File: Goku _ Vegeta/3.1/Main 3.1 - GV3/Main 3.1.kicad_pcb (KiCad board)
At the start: 2 copper layers, 215 x 206.6 mm, 43 parts, among them J1 JST-XH M1 ENC, J10 Conn_01x08_Female, J11 Motor Driver Inputs, J12 OpenMV H7, J13 JST-XH Screen, J14 Conn_01x08_Female, J15 691137710002, J16 691137710002, J17 Conn_01x08_Female, J18 Conn_01x18_Female, J19 Conn_01x10_Female, J2 JST-XH M2 ENC, J20 Conn_01x08_Female, J21 Conn_01x08_Female, J22 Conn_01x18_Female, J23 Line PCB 2, J24 B3B-XH-A(LF)(SN), J25 B2B-XH-A(LF)(SN), J3 JST-XH M3 ENC, J4 JST-XH M4 ENC, J5 XT60-M, J6 691137710002, J7 XT60-M, J8 XT60-M, J9 Line PCB 1, U1 DC-DC_Buck_Converter_7-24V_to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, U4 Adafruit_BNO055_STEMMA_QT

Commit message: move to 3.1
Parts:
- removed C3, C4: 10UF, Capacitor_SMD:C_0805_2012Metric
- removed G*** (x3): LOGO, LOGO
- removed J14, J17, J20, J21: Conn_01x08_Female, Connector_PinHeader_2.54mm:PinHeader_1x08_P2.54mm_Vertical
- removed J15, J16: 691137710002, 5mm Pitch 2-Pin Screw Terminal Block:5mm Pitch 2-Pin Screw Terminal Block
- removed J18, J22: Conn_01x18_Female, Connector_PinHeader_2.54mm:PinHeader_1x18_P2.54mm_Vertical
- removed J19: Conn_01x10_Female, Connector_PinHeader_2.54mm:PinHeader_1x10_P2.54mm_Vertical
- removed J23: Line PCB 2, Box IDC header 2x3:Box IDC header 2x3
- removed J24: B3B-XH-A(LF)(SN), B3B-XH-A_LF__SN_:JST_B3B-XH-A(LF)(SN)
- removed J25: B2B-XH-A(LF)(SN), B2B-XH-A_LF__SN_:JST_B2B-XH-A(LF)(SN)
- removed J5: XT60-M, XT60-M:XT60-M
- removed TP1: TestPoint - 5V, TestPoint:TestPoint_THTPad_D2.0mm_Drill1.0mm
- removed TP18: LOGIC_SWITCH, TestPoint:TestPoint_THTPad_D2.0mm_Drill1.0mm
- removed TP2: TestPoint - SCL, TestPoint:TestPoint_THTPad_D2.0mm_Drill1.0mm
- removed TP3: TestPoint - SDA, TestPoint:TestPoint_THTPad_D2.0mm_Drill1.0mm
- removed TP4: TestPoint - TX, TestPoint:TestPoint_THTPad_D2.0mm_Drill1.0mm
- removed TP5: TestPoint - RX, TestPoint:TestPoint_THTPad_D2.0mm_Drill1.0mm
- removed TP6: TestPoint - GND, TestPoint:TestPoint_THTPad_D2.0mm_Drill1.0mm
- added A10: ALS-PT19-315C/L177/TR8, ALS-PT19-315C_L177_TR8:XDCR_ALS-PT19-315C_L177_TR8, B.Cu at (164.1, 135.9)
- added A11: ALS-PT19-315C/L177/TR8, ALS-PT19-315C_L177_TR8:XDCR_ALS-PT19-315C_L177_TR8, B.Cu at (170.0, 150.0)
- added A12: ALS-PT19-315C/L177/TR8, ALS-PT19-315C_L177_TR8:XDCR_ALS-PT19-315C_L177_TR8, B.Cu at (164.1, 164.1)
- added A13: ALS-PT19-315C/L177/TR8, ALS-PT19-315C_L177_TR8:XDCR_ALS-PT19-315C_L177_TR8, B.Cu at (150.0, 170.0)
- added A14: ALS-PT19-315C/L177/TR8, ALS-PT19-315C_L177_TR8:XDCR_ALS-PT19-315C_L177_TR8, B.Cu at (135.9, 164.1)
- added A15: ALS-PT19-315C/L177/TR8, ALS-PT19-315C_L177_TR8:XDCR_ALS-PT19-315C_L177_TR8, B.Cu at (130.0, 150.0)
- added A16: ALS-PT19-315C/L177/TR8, ALS-PT19-315C_L177_TR8:XDCR_ALS-PT19-315C_L177_TR8, B.Cu at (135.9, 135.9)
- added A2: ALS-PT19-315C/L177/TR8, ALS-PT19-315C_L177_TR8:XDCR_ALS-PT19-315C_L177_TR8, B.Cu at (230.0, 150.0)
- added A3: ALS-PT19-315C/L177/TR8, ALS-PT19-315C_L177_TR8:XDCR_ALS-PT19-315C_L177_TR8, B.Cu at (150.0, 230.0)
- added A4: ALS-PT19-315C/L177/TR8, ALS-PT19-315C_L177_TR8:XDCR_ALS-PT19-315C_L177_TR8, B.Cu at (70.0, 150.0)
- added A5: ALS-PT19-315C/L177/TR8, ALS-PT19-315C_L177_TR8:XDCR_ALS-PT19-315C_L177_TR8, B.Cu at (150.0, 100.0)
- added A6: ALS-PT19-315C/L177/TR8, ALS-PT19-315C_L177_TR8:XDCR_ALS-PT19-315C_L177_TR8, B.Cu at (200.0, 150.0)
- added A7: ALS-PT19-315C/L177/TR8, ALS-PT19-315C_L177_TR8:XDCR_ALS-PT19-315C_L177_TR8, B.Cu at (150.0, 200.0)
- added A8: ALS-PT19-315C/L177/TR8, ALS-PT19-315C_L177_TR8:XDCR_ALS-PT19-315C_L177_TR8, B.Cu at (100.0, 150.0)
- added A9: ALS-PT19-315C/L177/TR8, ALS-PT19-315C_L177_TR8:XDCR_ALS-PT19-315C_L177_TR8, B.Cu at (150.0, 130.0)
- added C10: 1uF, Capacitor_SMD:C_0805_2012Metric, F.Cu at (148.2, 145.6)
- added C11: 100uF, Capacitor_THT:CP_Radial_D10.0mm_P5.00mm, F.Cu at (184.6, 85.0)
- added C12: 560uF, Capacitor_THT:CP_Radial_D18.0mm_P7.50mm, F.Cu at (124.8, 84.5)
- added C13: 560uF, Capacitor_THT:CP_Radial_D18.0mm_P7.50mm, F.Cu at (175.2, 84.5)
- added C14: 100uF, Capacitor_THT:CP_Radial_D10.0mm_P5.00mm, F.Cu at (115.4, 85.0)
- added C2: 100uF, Capacitor_THT:CP_Radial_D10.0mm_P5.00mm, F.Cu at (165.6, 197.0)
- added C9: 100uF, Capacitor_THT:CP_Radial_D10.0mm_P5.00mm, F.Cu at (152.4, 162.5)
- added D3: SS510, Diode_SMD:D_SMC, F.Cu at (144.2, 151.8)
- added D4: STTH2002G-TR, Package_TO_SOT_SMD:TO-263-2, F.Cu at (168.0, 100.2)
- added L3: 56uH, Inductor_SMD:L_Bourns_SRR1260, F.Cu at (134.0, 150.0)
- added LED1: JB2835AWT-W-U30GA0000-N0000001, JB2835AWT-W-U30GA0000-N0000001:LED_J2835_CRW, B.Cu at (150.0, 73.0)
- added LED10: JB2835AWT-W-U30GA0000-N0000001, JB2835AWT-W-U30GA0000-N0000001:LED_J2835_CRW, B.Cu at (162.0, 138.0)
- added LED11: JB2835AWT-W-U30GA0000-N0000001, JB2835AWT-W-U30GA0000-N0000001:LED_J2835_CRW, B.Cu at (167.0, 150.0)
- added LED12: JB2835AWT-W-U30GA0000-N0000001, JB2835AWT-W-U30GA0000-N0000001:LED_J2835_CRW, B.Cu at (162.0, 162.0)
- added LED13: JB2835AWT-W-U30GA0000-N0000001, JB2835AWT-W-U30GA0000-N0000001:LED_J2835_CRW, B.Cu at (150.0, 167.0)
- added LED14: JB2835AWT-W-U30GA0000-N0000001, JB2835AWT-W-U30GA0000-N0000001:LED_J2835_CRW, B.Cu at (138.0, 162.0)
- added LED15: JB2835AWT-W-U30GA0000-N0000001, JB2835AWT-W-U30GA0000-N0000001:LED_J2835_CRW, B.Cu at (133.0, 150.0)
- added LED16: JB2835AWT-W-U30GA0000-N0000001, JB2835AWT-W-U30GA0000-N0000001:LED_J2835_CRW, B.Cu at (138.0, 138.0)
- added LED2: JB2835AWT-W-U30GA0000-N0000001, JB2835AWT-W-U30GA0000-N0000001:LED_J2835_CRW, B.Cu at (227.0, 150.0)
- added LED3: JB2835AWT-W-U30GA0000-N0000001, JB2835AWT-W-U30GA0000-N0000001:LED_J2835_CRW, B.Cu at (150.0, 227.0)
- added LED4: JB2835AWT-W-U30GA0000-N0000001, JB2835AWT-W-U30GA0000-N0000001:LED_J2835_CRW, B.Cu at (73.0, 150.0)
- added LED5: JB2835AWT-W-U30GA0000-N0000001, JB2835AWT-W-U30GA0000-N0000001:LED_J2835_CRW, B.Cu at (150.0, 103.0)
- added LED6: JB2835AWT-W-U30GA0000-N0000001, JB2835AWT-W-U30GA0000-N0000001:LED_J2835_CRW, B.Cu at (197.0, 150.0)
- added LED7: JB2835AWT-W-U30GA0000-N0000001, JB2835AWT-W-U30GA0000-N0000001:LED_J2835_CRW, B.Cu at (150.0, 197.0)
- added LED8: JB2835AWT-W-U30GA0000-N0000001, JB2835AWT-W-U30GA0000-N0000001:LED_J2835_CRW, B.Cu at (103.0, 150.0)
- added LED9: JB2835AWT-W-U30GA0000-N0000001, JB2835AWT-W-U30GA0000-N0000001:LED_J2835_CRW, B.Cu at (150.0, 133.0)
- added Q1: BSC040N10NS5, Package_TO_SOT_SMD:TDSON-8-1, F.Cu at (133.2, 108.0)
- added R1: 12R, Resistor_SMD:R_0805_2012Metric, B.Cu at (154.0, 73.0)
- added R10: 10K, Resistor_SMD:R_0805_2012Metric, B.Cu at (227.0, 146.0)
- added R11: 10K, Resistor_SMD:R_0805_2012Metric, B.Cu at (154.0, 227.0)
- added R12: 10K, Resistor_SMD:R_0805_2012Metric, B.Cu at (73.0, 154.0)
- added R15: 10K, Resistor_SMD:R_0805_2012Metric, B.Cu at (154.0, 197.0)
- added R16: 10K, Resistor_SMD:R_0805_2012Metric, B.Cu at (103.0, 154.0)
- added R17: 12R, Resistor_SMD:R_0805_2012Metric, B.Cu at (154.0, 133.0)
- added R18: 12R, Resistor_SMD:R_0805_2012Metric, B.Cu at (164.8, 140.8)
- added R19: 12R, Resistor_SMD:R_0805_2012Metric, B.Cu at (167.0, 154.0)
- added R2: 12R, Resistor_SMD:R_0805_2012Metric, B.Cu at (227.0, 154.0)
- added R20: 12R, Resistor_SMD:R_0805_2012Metric, B.Cu at (159.2, 164.8)
- added R21: 12R, Resistor_SMD:R_0805_2012Metric, B.Cu at (146.0, 167.0)
- added R22: 12R, Resistor_SMD:R_0805_2012Metric, B.Cu at (135.2, 159.2)
- added R23: 12R, Resistor_SMD:R_0805_2012Metric, B.Cu at (133.0, 146.0)
- added R24: 12R, Resistor_SMD:R_0805_2012Metric, B.Cu at (140.8, 135.2)
- added R25: 10K, Resistor_SMD:R_0805_2012Metric, B.Cu at (146.0, 133.0)
- added R26: 10K, Resistor_SMD:R_0805_2012Metric, B.Cu at (159.2, 135.2)
- added R27: 10K, Resistor_SMD:R_0805_2012Metric, B.Cu at (167.0, 146.0)
- added R28: 10K, Resistor_SMD:R_0805_2012Metric, B.Cu at (164.8, 159.2)
- added R29: 10K, Resistor_SMD:R_0805_2012Metric, B.Cu at (154.0, 167.0)
- added R3: 12R, Resistor_SMD:R_0805_2012Metric, B.Cu at (146.0, 227.0)
- added R30: 10K, Resistor_SMD:R_0805_2012Metric, B.Cu at (140.8, 164.8)
- added R31: 10K, Resistor_SMD:R_0805_2012Metric, B.Cu at (133.0, 154.0)
- added R32: 10K, Resistor_SMD:R_0805_2012Metric, B.Cu at (135.2, 140.8)
- added R35: 2K94, Resistor_SMD:R_0805_2012Metric, F.Cu at (151.7, 145.6)
- added R36: 1K5, Resistor_SMD:R_0805_2012Metric, F.Cu at (151.7, 156.1)
- added R37: CT6EP103, POT_CT-6EP_NDC:POT_CT-6EP_NDC, F.Cu at (159.8, 141.4)
- added R38: 57K, Resistor_SMD:R_0805_2012Metric, F.Cu at (148.2, 143.6)
- added R4: 12R, Resistor_SMD:R_0805_2012Metric, B.Cu at (73.0, 146.0)
- added R5: 12R, Resistor_SMD:R_0805_2012Metric, B.Cu at (154.0, 103.0)
- added R6: 12R, Resistor_SMD:R_0805_2012Metric, B.Cu at (197.0, 154.0)
- added R7: 12R, Resistor_SMD:R_0805_2012Metric, B.Cu at (146.0, 197.0)
- added R8: 12R, Resistor_SMD:R_0805_2012Metric, B.Cu at (103.0, 146.0)
- added R9: 10K, Resistor_SMD:R_0805_2012Metric, B.Cu at (146.0, 73.0)
- added U2: ~, Converter_DCDC:DC-DC Multi-output Buck Converter, F.Cu at (163.3, 230.0)
- added U3: LM2587S-ADJ, LM2587S-ADJ:VREG_TPS79625KTTR, F.Cu at (160.6, 150.9)
- added U5: TB67H420FTG Dual/Single Motor Driver Carrier, TB67H420FTG Dual_Single Motor Driver Carrier:TB67H420FTG DualSingle Motor Driver Carrier, F.Cu at (200.0, 150.0)
- added U6: TB67H420FTG Dual/Single Motor Driver Carrier, TB67H420FTG Dual_Single Motor Driver Carrier:TB67H420FTG DualSingle Motor Driver Carrier, F.Cu at (100.0, 150.0)
- added U7: TB67H420FTG Dual/Single Motor Driver Carrier, TB67H420FTG Dual_Single Motor Driver Carrier:TB67H420FTG DualSingle Motor Driver Carrier, F.Cu at (70.0, 150.0)
- added U8: DEV-16771, DEV-16771:MODULE_DEV-16771, F.Cu at (150.0, 218.0)
- A1: value A000067 -> ALS-PT19-315C/L177/TR8; footprint A000067:ARDUINO_A000067_FLIPPED -> ALS-PT19-315C_L177_TR8:XDCR_ALS-PT19-315C_L177_TR8; moved to B.Cu
- C1: value 10UF -> 100uF; footprint Capacitor_SMD:C_0805_2012Metric -> Capacitor_THT:CP_Radial_D10.0mm_P5.00mm
- J1: value JST-XH M1 ENC -> BATTERY POWER; footprint B4B-XH-A_LF__SN_:JST_B4B-XH-A(LF)(SN) -> Connector_AMASS:AMASS_XT30U-F_1x02_P5.0mm_Vertical
- J10: value Conn_01x08_Female -> Motor 4; footprint Connector_PinHeader_2.54mm:PinHeader_1x08_P2.54mm_Vertical -> Connector_PinSocket_2.54mm:PinSocket_1x06_P2.54mm_Vertical
- J11: value Motor Driver Inputs -> LEFT HEADERS; footprint Box IDC header 2x5:Box IDC header 2x5 -> Connector_PinHeader_2.54mm:PinHeader_1x24_P2.54mm_Vertical
- J12: value OpenMV H7 -> RIGHT HEADERS; footprint Box IDC header 2x3:Box IDC header 2x3 -> Connector_PinHeader_2.54mm:PinHeader_1x24_P2.54mm_Vertical
- J13: value JST-XH Screen -> MID HEADERS; footprint B4B-XH-A_LF__SN_:JST_B4B-XH-A(LF)(SN) -> Connector_PinHeader_2.54mm:PinHeader_1x05_P2.54mm_Vertical
- J2: value JST-XH M2 ENC -> BACKUP 5V; footprint B4B-XH-A_LF__SN_:JST_B4B-XH-A(LF)(SN) -> Connector_AMASS:AMASS_XT30U-F_1x02_P5.0mm_Vertical
- J3: value JST-XH M3 ENC -> BACKUP 3V3; footprint B4B-XH-A_LF__SN_:JST_B4B-XH-A(LF)(SN) -> Connector_AMASS:AMASS_XT30U-F_1x02_P5.0mm_Vertical
- J4: value JST-XH M4 ENC -> I2C; footprint B4B-XH-A_LF__SN_:JST_B4B-XH-A(LF)(SN) -> Connector_AMASS:AMASS_XT30U-F_1x02_P5.0mm_Vertical
- J6: value 691137710002 -> Solenoid; footprint 5mm Pitch 2-Pin Screw Terminal Block:5mm Pitch 2-Pin Screw Terminal Block -> TerminalBlock:TerminalBlock_bornier-2_P5.08mm
- J7: value XT60-M -> Motor 1; footprint XT60-M:XT60-M -> Connector_PinSocket_2.54mm:PinSocket_1x06_P2.54mm_Vertical
- J8: value XT60-M -> Motor 2; footprint XT60-M:XT60-M -> Connector_PinSocket_2.54mm:PinSocket_1x06_P2.54mm_Vertical
- J9: value Line PCB 1 -> Motor 3; footprint Box IDC header 2x3:Box IDC header 2x3 -> Connector_PinSocket_2.54mm:PinSocket_1x06_P2.54mm_Vertical
- R13, R14: moved to B.Cu
- U1: value DC-DC_Buck_Converter_7-24V_to_5V_4A -> ~; footprint 2.3 PCBs:DC-DC_Buck_Converter_7-24V_to_5V_4A -> Converter_DCDC:DC-DC Multi-output Buck Converter
- U4: value Adafruit_BNO055_STEMMA_QT -> TB67H420FTG Dual/Single Motor Driver Carrier; footprint 2.3 PCBs:Adafruit IMU BNO055 -> TB67H420FTG Dual_Single Motor Driver Carrier:TB67H420FTG DualSingle Motor Driver Carrier
- moved J10 138.9 mm to (95.5, 120.5), turned to 45 degrees
- moved J4 128.9 mm to (78.8, 175.5), turned to 0 degrees
- moved J6 124.8 mm to (128.5, 101.6), turned to 90 degrees
- moved J1 121.6 mm to (78.8, 124.5)
- moved U4 111.4 mm to (230.0, 150.0), turned to 0 degrees
- moved J11 96.9 mm to (161.0, 247.2), turned to 180 degrees
- moved R14 90.6 mm to (197.0, 146.0), turned to 0 degrees
- moved J7 89.2 mm to (204.5, 120.5), turned to -45 degrees
- moved C1 88.3 mm to (128.6, 197.0), turned to 0 degrees
- moved J13 88.1 mm to (144.9, 183.5)
- moved J12 82.8 mm to (139.0, 247.2), turned to 180 degrees
- moved U1 81.0 mm to (116.8, 230.0), turned to 90 degrees
- moved A1 61.0 mm to (150.0, 70.0), turned to 180 degrees
- moved J8 53.5 mm to (204.5, 179.5), turned to -135 degrees
- moved J2 45.1 mm to (221.2, 124.5), turned to 180 degrees
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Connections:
- A1 pad 1: Net-(A1-Pad1) -> +3V3
- A1 pad 2: /M3ENCA -> /21
- C1 pad 1: +5V -> GND
- C1 pad 2: GND -> +3V3
- J1 pad 1: /M1ENCB -> GND
- J1 pad 2: /M1ENCA -> +15V
- J10 pad 1: Net-(A1-PadNC) -> Net-(J10-Pin_1)
- J10 pad 2: Net-(A1-PadIOREF) -> Net-(J10-Pin_2)
- J10 pad 3: Net-(A1-PadRESET) -> GND
- J10 pad 4: Net-(A1-Pad3V3) -> +3V3
- J10 pad 5: +5V -> /32
- J10 pad 6: GND -> /28
- J11 pad 1: /DIR1 (1) -> GND
- J11 pad 10: GND -> /8
- J11 pad 2: /PWM1 (1) -> /0
- J11 pad 3: /DIR2 (2) -> /1
- J11 pad 4: /PWM2 (2) -> /2
- J11 pad 5: GND -> /3
- J11 pad 6: /DIR1 (3) -> /4
- J11 pad 7: /PWM1 (3) -> /5
- J11 pad 8: /DIR2 (4) -> /6
- J11 pad 9: /PWM2 (4) -> /7
- J12 pad 3: /TX -> +3V3
- J12 pad 4: /RX -> /23
- J12 pad 5: unconnected-(J12-Pad5) -> /22
- J12 pad 6: unconnected-(J12-Pad6) -> /21
- J13 pad 1: +5V -> /ON/OFF
- J13 pad 2: GND -> /PROGRAM
- J13 pad 3: /SCL -> GND
- J13 pad 4: /SDA -> unconnected-(J13-Pin_4-Pad4)
- J2 pad 1: /M2ENCB -> GND
- J2 pad 2: /M2ENCA -> +5V
- J3 pad 1: /M3ENCB -> GND
- J3 pad 2: /M3ENCA -> +3V3
- J4 pad 1: /M4ENCB -> /19
- J4 pad 2: /M4ENCA -> /18
- J6 pad 1: +15V -> Net-(D3-K)
- J6 pad 2: GND -> Net-(D4-K)
- J9 pad 1: Net-(A1-PadAD0) -> Net-(J9-Pin_1)
- J9 pad 2: Net-(A1-PadAD1) -> Net-(J9-Pin_2)
- J9 pad 3: Net-(A1-PadAD2) -> GND
- J9 pad 4: Net-(A1-PadAD3) -> +3V3
- J9 pad 5: Net-(A1-PadAD4) -> /34
- J9 pad 6: Net-(A1-PadAD5) -> /33
- R13 pad 1: /SCL -> GND
- R13 pad 2: +5V -> /20
- R14 pad 1: /SDA -> GND
- R14 pad 2: +5V -> /27
- U1 pad 4: +5V -> +3V3
- U4 pad 1: +5V -> unconnected-(U4-VM-Pad1)
- U4 pad 2: unconnected-(U4-Pad2) -> GND
- U4 pad 3: GND -> unconnected-(U4-VCC-Pad3)
- U4 pad 4: /SCL -> /4
- U4 pad 5: /SDA -> /3
- U4 pad 6: /RST -> /2
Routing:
- net +3V3: track 0.00 -> 760.4 mm, vias 0 -> 13
- net Net-(J7-PadN): track 239.2 -> 0.00 mm
- net Net-(D3-K): track 0.00 -> 200.8 mm, vias 0 -> 3
- net /SDA: track 192.6 -> 0.00 mm, vias 1 -> 0
- net /21: track 0.00 -> 190.6 mm
- net +5V: track 30.4 -> 220.0 mm, vias 1 -> 0
- net /SCL: track 179.9 -> 0.00 mm, vias 2 -> 0
- net /TX: track 168.8 -> 0.00 mm, vias 1 -> 0
- net /RX: track 165.6 -> 0.00 mm
- net Net-(A1-PadAD6): track 161.1 -> 0.00 mm
- net Net-(A1-PadAD7): track 156.3 -> 0.00 mm
- net Net-(A1-PadAD3): track 152.7 -> 0.00 mm
- net Net-(A1-PadAD0): track 152.4 -> 0.00 mm
- net /20: track 0.00 -> 152.0 mm
- net Net-(A1-PadAD8): track 151.5 -> 0.00 mm, vias 2 -> 0
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- added copper zone on F.Cu, net +15V
- added copper zone on B.Cu, net GND
- removed copper zone on B.Cu, net +5V
- removed copper zone on F.Cu, net GND
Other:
- board size 215 x 206.6 mm -> 206 x 197.4 mm
- board text added: "Designed by Hugh Phan - September 2023"
- board text added: "Fort Street's Team Silverback Hugh Phan Jayden Nguyen Issey Lee Jack Sumner KZ KC"
- board text added: "MOTOR A"
- board text added: "MOTOR B"
- board text added: "MOTOR C"
- board text added: "MOTOR D"
- board text added: "TEENSY 4.1 3V3 LINES NOT CONNECTED"
- board text removed: "15V"
- board text removed: "3V3"
- board text removed: "5V"
- board text removed: "Designed by Hugh Phan 9/07/2023"
- board text removed: "Fort Street Team Silverback 2023 Hugh Phan Issey Lee Jayden Nguyen Jack Sumner"
- board text removed: "G V 2"
- board text removed: "GND"
- board text removed: "LINE PCB"
- board text removed: "LOGIC"
- board text removed: "MAIN 2.4 PCB"
- board text removed: "RX"
- board text removed: "SCL"
- board text removed: "SDA"
- board text removed: "SEN1"
- board text removed: "TX"
- board text removed: "X"

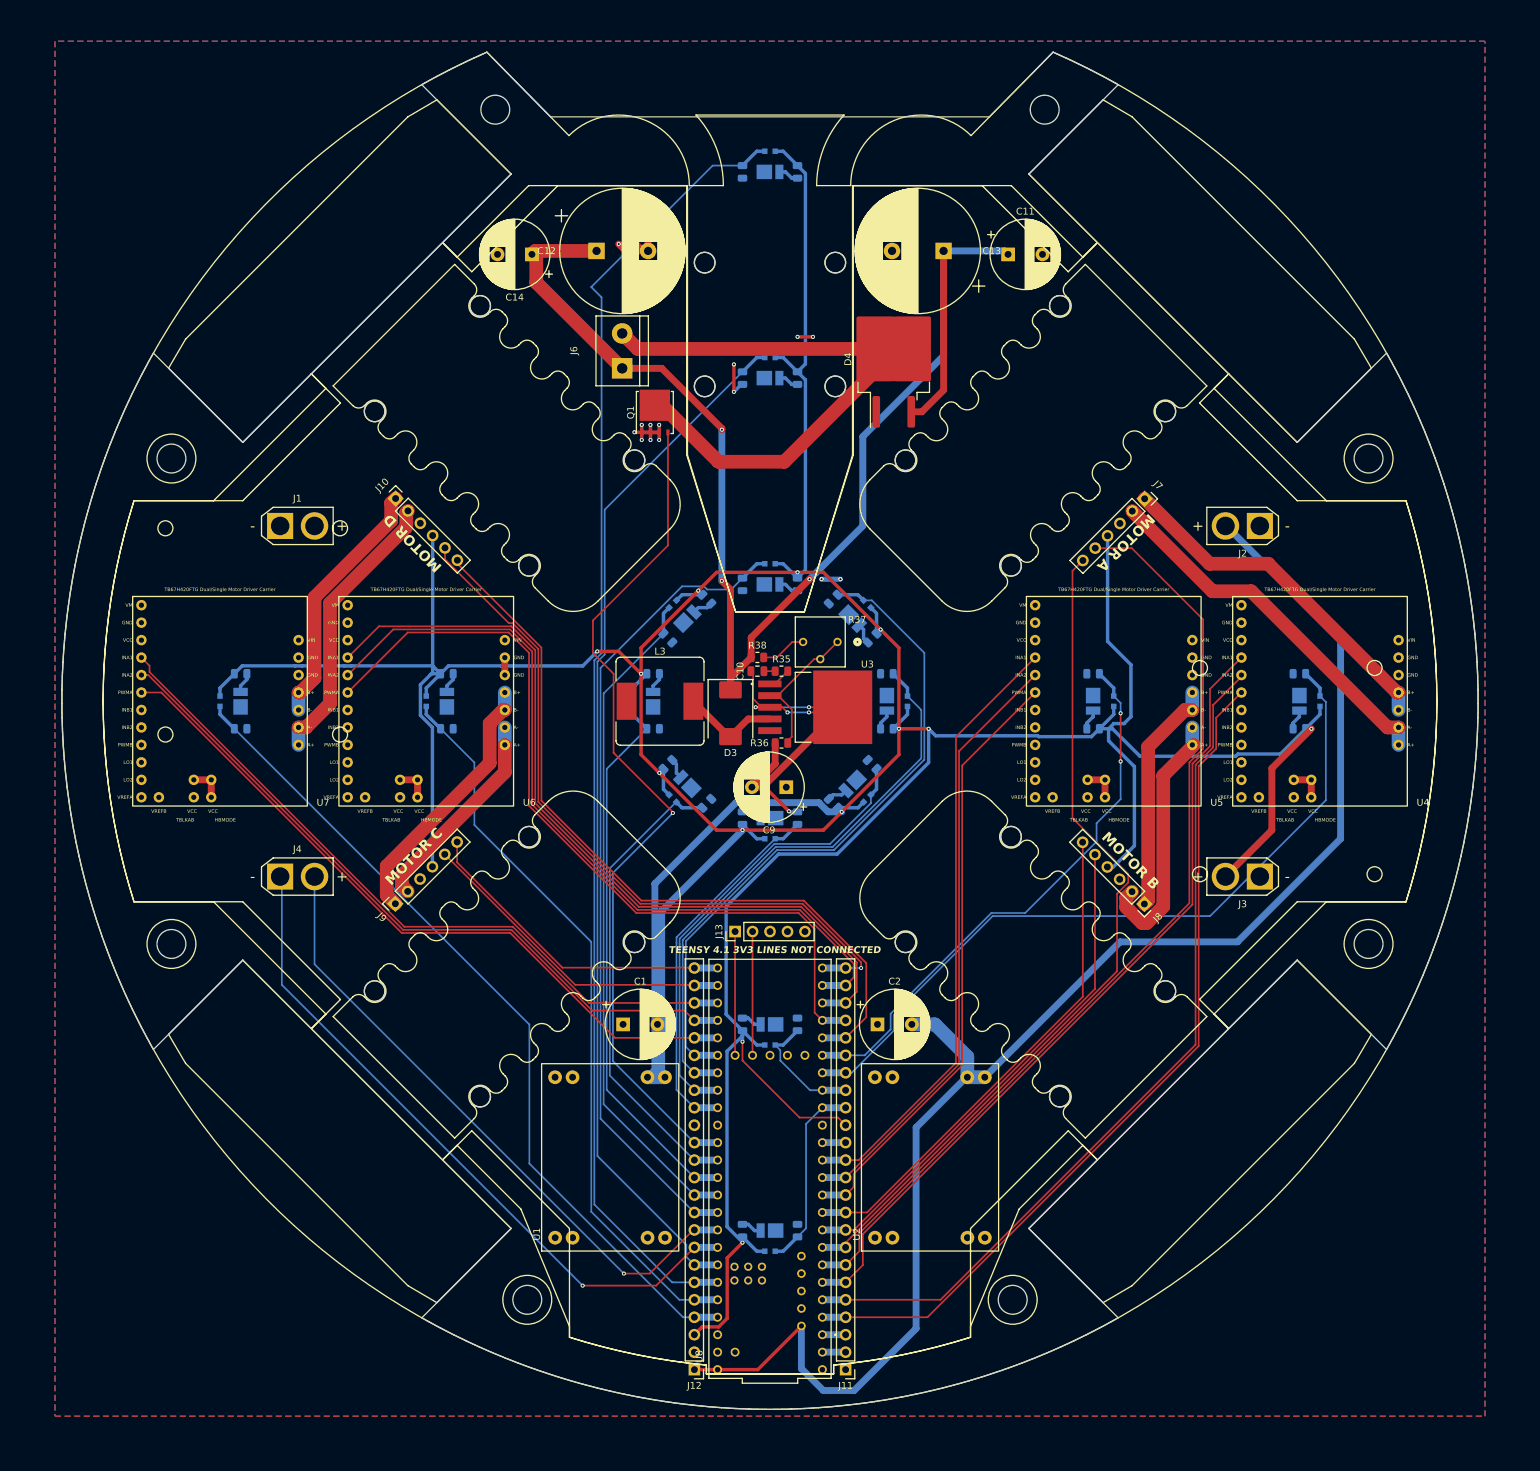
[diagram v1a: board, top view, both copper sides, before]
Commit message: MAIN 3.1 DONE no silkscreen
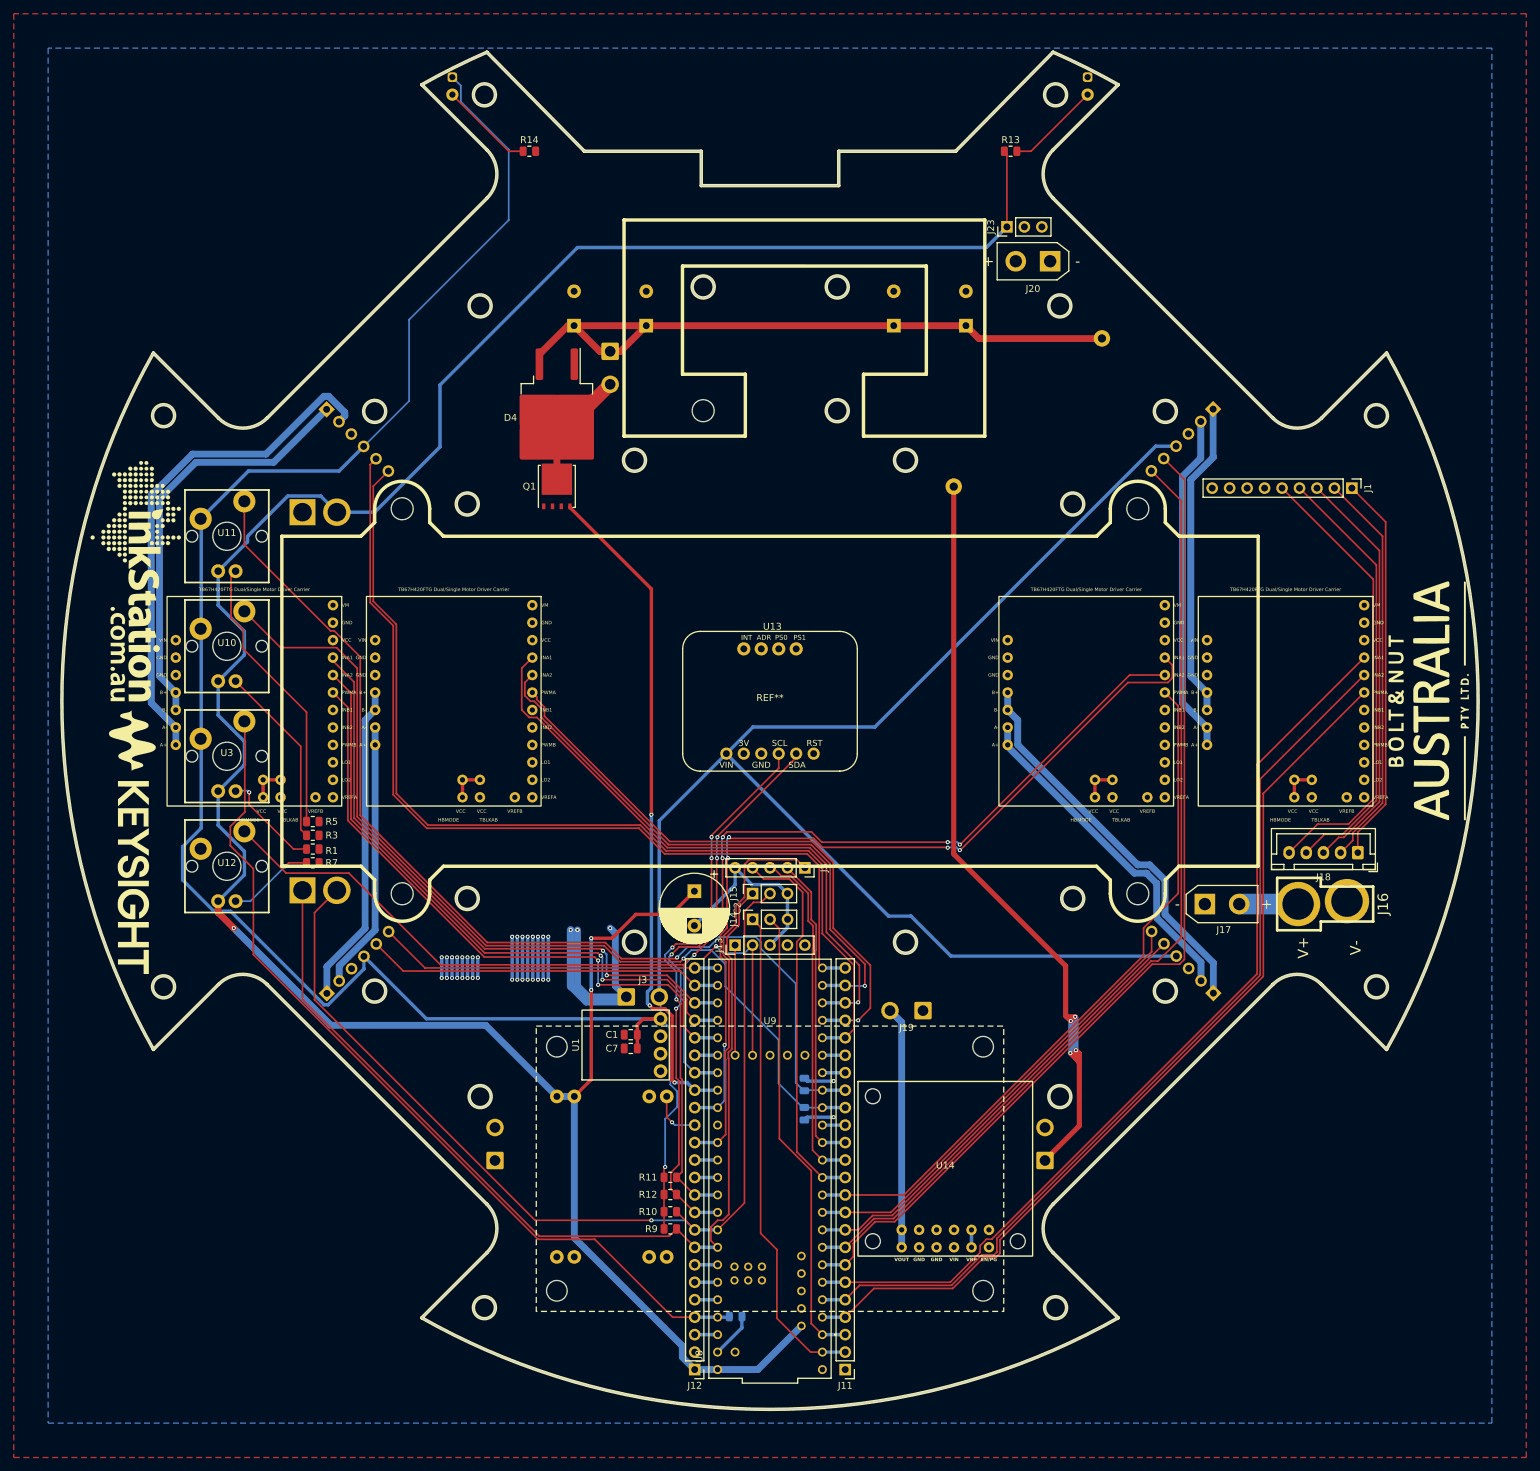
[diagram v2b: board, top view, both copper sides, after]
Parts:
- removed A1, A10, A11, A12, A13, A14, A15, A16, A2, A3, A4, A5, A6, A7, A8, A9: ALS-PT19-315C/L177/TR8, ALS-PT19-315C_L177_TR8:XDCR_ALS-PT19-315C_L177_TR8
- removed C10: 1uF, Capacitor_SMD:C_0805_2012Metric
- removed C11, C14, C9: 100uF, Capacitor_THT:CP_Radial_D10.0mm_P5.00mm
- removed C12, C13: 560uF, Capacitor_THT:CP_Radial_D18.0mm_P7.50mm
- removed D3: SS510, Diode_SMD:D_SMC
- removed L3: 56uH, Inductor_SMD:L_Bourns_SRR1260
- removed LED1, LED10, LED11, LED12, LED13, LED14, LED15, LED16, LED2, LED3, LED4, LED5, LED6, LED7, LED8, LED9: JB2835AWT-W-U30GA0000-N0000001, JB2835AWT-W-U30GA0000-N0000001:LED_J2835_CRW
- removed R16, R25, R26, R27, R28, R29, R30, R31, R32: 10K, Resistor_SMD:R_0805_2012Metric
- removed R17, R18, R19, R20, R21, R22, R23, R24, R8: 12R, Resistor_SMD:R_0805_2012Metric
- removed R35: 2K94, Resistor_SMD:R_0805_2012Metric
- removed R36: 1K5, Resistor_SMD:R_0805_2012Metric
- removed R37: CT6EP103, POT_CT-6EP_NDC:POT_CT-6EP_NDC
- removed R38: 57K, Resistor_SMD:R_0805_2012Metric
- added C3: 750uF, Capacitor_THT:CP_Radial_D10.0mm_P5.00mm, B.Cu at (121.5, 95.4)
- added C4: 750uF, Capacitor_THT:CP_Radial_D10.0mm_P5.00mm, B.Cu at (132.0, 95.4)
- added C5: 750uF, Capacitor_THT:CP_Radial_D10.0mm_P5.00mm, B.Cu at (168.0, 95.4)
- added C6: 750uF, Capacitor_THT:CP_Radial_D10.0mm_P5.00mm, B.Cu at (178.5, 95.4)
- added C7: 10uF, Capacitor_SMD:C_0805_2012Metric, F.Cu at (129.8, 200.5)
- added D1: LED, LED_THT:LED_D3.0mm, B.Cu at (196.2, 59.2)
- added G***: LOGO, LOGO, F.Cu at (245.5, 150.0)
- added G***: LOGO, LOGO, F.Cu at (57.2, 170.5)
- added G***: LOGO, LOGO, F.Cu at (57.8, 132.5)
- added J14: UART, Connector_PinSocket_2.54mm:PinSocket_1x03_P2.54mm_Vertical, F.Cu at (147.5, 181.7)
- added J15: I2C, Connector_PinSocket_2.54mm:PinSocket_1x03_P2.54mm_Vertical, F.Cu at (147.5, 178.0)
- added J16: 4S Battery, Connectors:DEANS, F.Cu at (231.4, 179.5)
- added J17: Power Switch, Connector_AMASS:AMASS_XT30UPB-F_1x02_P5.0mm_Vertical, F.Cu at (213.2, 179.5)
- added J18: Batt Bal, Connector_JST:JST_XH_B5B-XH-A_1x05_P2.50mm_Vertical, F.Cu at (235.5, 172.0)
- added J19: 5V PI, Connector_Wire:SolderWire-0.75sqmm_1x02_P4.8mm_D1.25mm_OD2.3mm, F.Cu at (172.2, 195.0)
- added J20: ESC PWR, Connector_AMASS:AMASS_XT30UPB-F_1x02_P5.0mm_Vertical, F.Cu at (190.8, 86.0)
- added J23: ESC PWM, Connector_PinHeader_2.54mm:PinHeader_1x03_P2.54mm_Vertical, F.Cu at (184.5, 81.0)
- added J5: SPI, Connector_PinSocket_2.54mm:PinSocket_1x05_P2.54mm_Vertical, F.Cu at (155.1, 174.2)
- added Q2: Q_Photo_NPN, LED_THT:LED_D3.0mm, B.Cu at (103.8, 59.2)
- added REF**: Main 3.1 3D Model, 2.3 PCBs:Main 3.1 3D Model, F.Cu at (150.0, 150.0)
- added U10: ~, Button_Switch_Keyboard:SW_Cherry_MX_3mmLED, F.Cu at (71.0, 142.0)
- added U11: ~, Button_Switch_Keyboard:SW_Cherry_MX_3mmLED, F.Cu at (71.0, 126.0)
- added U12: ~, Button_Switch_Keyboard:SW_Cherry_MX_3mmLED, F.Cu at (71.0, 174.0)
- added U13: Adafruit_BNO055_STEMMA_QT, 2.3 PCBs:Adafruit IMU BNO055, F.Cu at (150.0, 150.0)
- added U14: ~, Converter_DCDC:5V, 5.5A Step-Down Voltage Regulator D36V50F5, F.Cu at (175.5, 218.0)
- added U9: Arduino Compatible DC-DC Boost Module with Display, Converter_DCDC:Arduino Compatible DC-DC Boost Module with Display, F.Cu at (150.0, 218.0)
- C1: value 100uF -> 10uF; footprint Capacitor_THT:CP_Radial_D10.0mm_P5.00mm -> Capacitor_SMD:C_0805_2012Metric
- J1: value BATTERY POWER -> Battery Buzzer; footprint Connector_AMASS:AMASS_XT30U-F_1x02_P5.0mm_Vertical -> Connector_PinHeader_2.54mm:PinHeader_1x09_P2.54mm_Vertical
- J10, J4, J7, J8, J9, U2, U4, U5, U6, U7: moved to B.Cu
- J2: value BACKUP 5V -> 5V LINE; moved to B.Cu
- J3: footprint Connector_AMASS:AMASS_XT30U-F_1x02_P5.0mm_Vertical -> Connector_Wire:SolderWire-0.75sqmm_1x02_P4.8mm_D1.25mm_OD2.3mm
- J6: footprint TerminalBlock:TerminalBlock_bornier-2_P5.08mm -> Connector_Wire:SolderWire-0.75sqmm_1x02_P4.8mm_D1.25mm_OD2.3mm; moved to B.Cu
- R1, R3, R5, R7: value 12R -> 30R; moved to F.Cu
- R10, R11, R12, R14, R9: moved to F.Cu
- R13: value 10K -> 95R; moved to F.Cu
- R15: value 10K -> 4R7; footprint Resistor_SMD:R_0805_2012Metric -> Resistor_THT:R_Axial_Power_L25.0mm_W9.0mm_P30.48mm
- R2, R4, R6: value 12R -> 10K
- U1: footprint Converter_DCDC:DC-DC Multi-output Buck Converter -> Converter_DCDC:Pololu 3.3V, 500mA Step-Down Voltage Regulator D24V5F3
- U3: value LM2587S-ADJ -> ~; footprint LM2587S-ADJ:VREG_TPS79625KTTR -> Button_Switch_Keyboard:SW_Cherry_MX_3mmLED
- moved J1 156.0 mm to (234.6, 119.0), turned to -90 degrees
- moved R9 154.1 mm to (135.5, 226.8), turned to 180 degrees
- moved J2 139.3 mm to (82.0, 122.5), turned to 0 degrees
- moved R1 121.1 mm to (83.5, 171.5), turned to 180 degrees
- moved R10 120.4 mm to (135.5, 224.2), turned to 180 degrees
- moved R2 118.5 mm to (145.0, 239.5), turned to 0 degrees
- moved R14 111.8 mm to (115.0, 70.0)
- moved R15 109.2 mm to (198.3, 97.2), turned to -135 degrees
- moved R4 104.0 mm to (155.0, 210.0), turned to -90 degrees
- moved R5 95.6 mm to (83.5, 167.5), turned to 180 degrees
- moved J3 93.8 mm to (129.1, 193.0), turned to 0 degrees
- moved R12 92.2 mm to (135.5, 221.8)
- moved U3 89.9 mm to (71.0, 158.0)
- moved R3 84.9 mm to (83.5, 169.5), turned to 180 degrees
- moved R7 66.8 mm to (83.5, 173.5), turned to 180 degrees
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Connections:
- C1 pad 1: GND -> +3V3
- C1 pad 2: +3V3 -> GND
- C2 pad 1: GND -> +5V
- C2 pad 2: +5V -> GND
- D4 pad 3: Net-(D3-K) -> Net-(D4-A)
- J1 pad 1: GND -> Net-(J1-Pin_1)
- J1 pad 2: +15V -> Net-(J1-Pin_2)
- J11 pad 15: +3V3 -> /3.3V_1
- J12 pad 3: +3V3 -> /3.3V_2
- J6 pad 1: Net-(D3-K) -> Net-(D4-A)
- Q1 pad 4: /13 -> /40
- R1 pad 1: +3V3 -> GND
- R1 pad 2: Net-(LED1-Pad2) -> Net-(R1-Pad2)
- R10 pad 1: GND -> /18
- R10 pad 2: /26 -> +3V3
- R11 pad 1: GND -> /16
- R11 pad 2: /24 -> +3V3
- R12 pad 1: GND -> /17
- R12 pad 2: /23 -> +3V3
- R13 pad 1: GND -> +5V
- R13 pad 2: /20 -> Net-(D1-A)
- R14 pad 1: GND -> /LINE BREAK
- R14 pad 2: /27 -> GND
- R15 pad 1: GND -> Net-(D4-A)
- R15 pad 2: /25 -> Net-(U9-OUT+)
- R2 pad 1: +3V3 -> /23
- R2 pad 2: Net-(LED2-Pad2) -> GND
- R3 pad 1: +3V3 -> GND
- R4 pad 1: +3V3 -> /24
- R4 pad 2: Net-(LED4-Pad2) -> GND
- R5 pad 1: +3V3 -> GND
- R6 pad 1: +3V3 -> /25
- R6 pad 2: Net-(LED6-Pad2) -> GND
- R7 pad 1: +3V3 -> GND
- R9 pad 1: GND -> /19
- R9 pad 2: /21 -> +3V3
- U1 pad 1: GND -> unconnected-(U1-SHDN-Pad1)
- U5 pad 4: /11 -> /41
- U5 pad 5: /10 -> /39
- U8 pad 3.3V_1: unconnected-(U8-3.3V-Pad3.3V_1) -> /3.3V_1
- U8 pad 3.3V_2: unconnected-(U8-3.3V__1-Pad3.3V_2) -> /3.3V_2
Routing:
- net +3V3: track 760.4 -> 476.4 mm, vias 13 -> 1
- net Net-(D3-K): track 200.8 -> 0.00 mm, vias 3 -> 0
- net /21: track 190.6 -> 3.33 mm
- net +5V: track 220.0 -> 383.3 mm, vias 0 -> 3
- net /20: track 152.0 -> 3.33 mm
- net /25: track 18.0 -> 151.7 mm, vias 0 -> 1
- net Net-(U9-OUT+): track 0.00 -> 119.6 mm, vias 0 -> 4
- net /24: track 27.8 -> 137.1 mm, vias 0 -> 1
- net /26: track 110.6 -> 3.32 mm
- net /22: track 107.1 -> 3.33 mm
- net Net-(D4-A): track 0.00 -> 99.3 mm
- net /38: track 97.8 -> 3.33 mm
- net /PROGRAM: track 18.0 -> 100.0 mm, vias 0 -> 1
- net /27: track 81.2 -> 3.32 mm, vias 2 -> 0
- net /15: track 80.5 -> 3.33 mm
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- added copper zone on B.Cu, net +15V
- added copper zone on F.Cu, net GND
- removed copper zone on F.Cu, net +15V
- removed copper zone on B.Cu, net GND
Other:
- outline, holes or cut-outs redrawn
- board text removed: "Designed by Hugh Phan - September 2023"
- board text removed: "Fort Street's Team Silverback Hugh Phan Jayden Nguyen Issey Lee Jack Sumner KZ KC"
- board text removed: "MOTOR A"
- board text removed: "MOTOR B"
- board text removed: "MOTOR C"
- board text removed: "MOTOR D"
- board text removed: "TEENSY 4.1 3V3 LINES NOT CONNECTED"
